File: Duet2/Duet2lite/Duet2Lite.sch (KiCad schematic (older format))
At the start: 0 parts

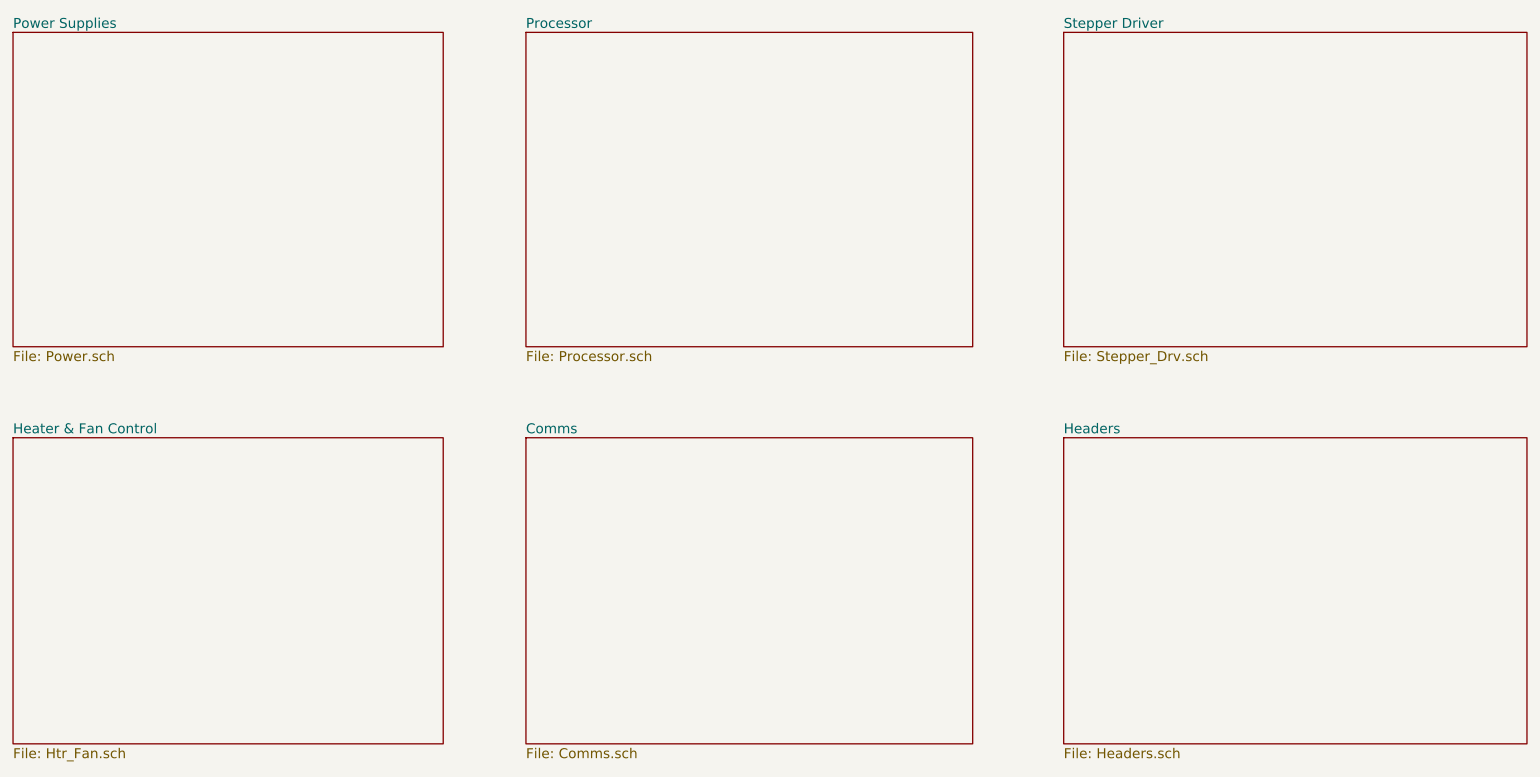
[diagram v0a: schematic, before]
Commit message: removed stepper drivers from the schematic
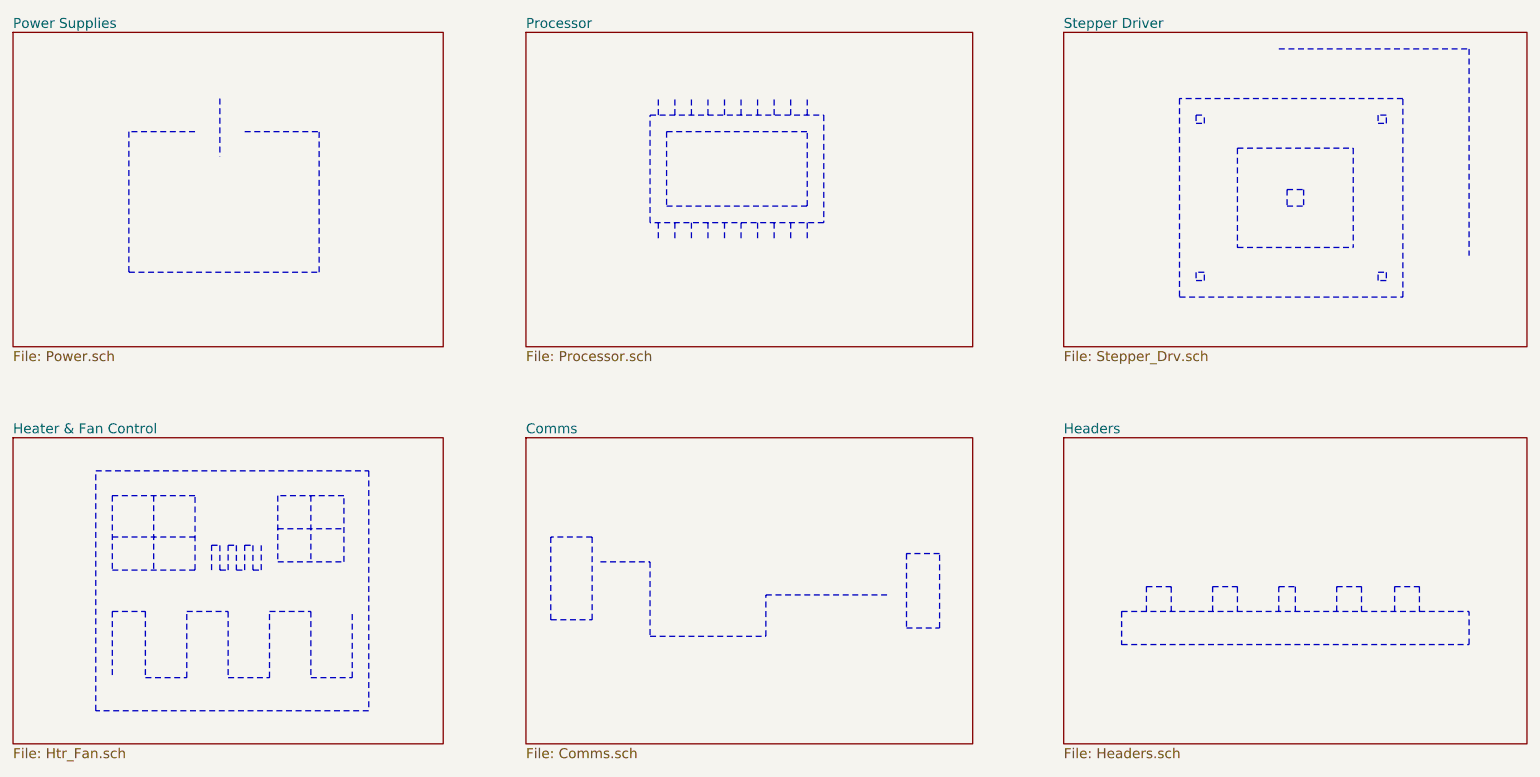
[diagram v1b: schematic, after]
